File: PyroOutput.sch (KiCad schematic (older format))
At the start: 9 parts, among them J11 PYRO 1, U11 TPS1HC100

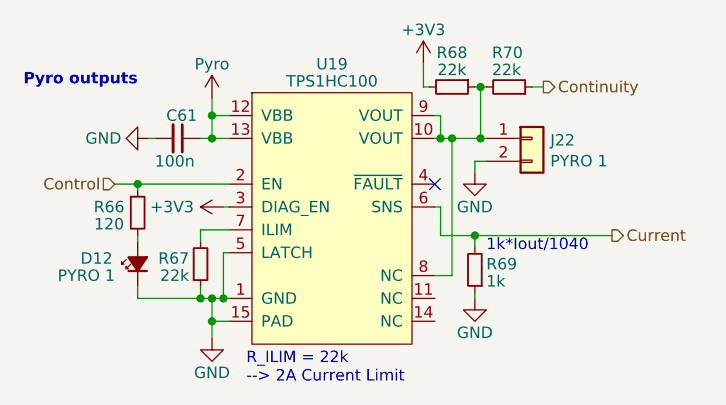
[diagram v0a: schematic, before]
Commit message: changed form factor to better fit into uHb engine section
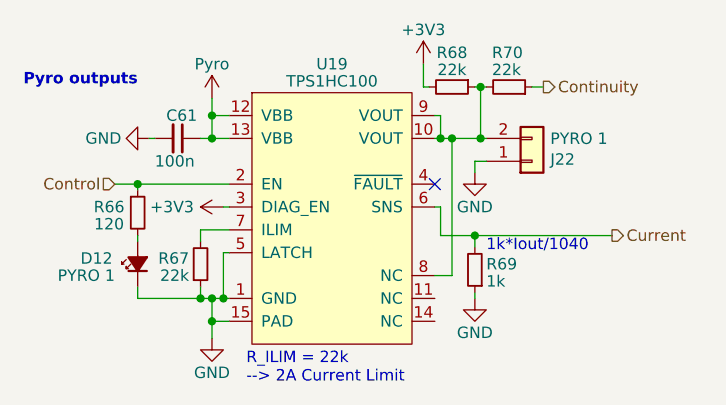
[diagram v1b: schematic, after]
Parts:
- J11: footprint TXV_LIB:Molex_SL_1x2 -> TXV_LIB:Molex_SL_1x2_Vertical
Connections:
- net GND: now also J11.1 (Pin_1); no longer J11.2 (Pin_2)
- net at R34.1, R36.2, U11.10 (VOUT)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: now also J11.2 (Pin_2); no longer J11.1 (Pin_1)
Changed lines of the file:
@@
 L Connector_Generic:Conn_01x02 J?
 U 1 1 639C46E3
-P 6550 3875
+P 6550 3975
 AR Path="/639C46E3" Ref="J?"  Part="1"
 AR Path="/638A960E/639C46E3" Ref="J11"  Part="1"
 AR Path="/64156100/639C46E3" Ref="J21"  Part="1"
 AR Path="/6419F64A/639C46E3" Ref="J22"  Part="1"
-F 0 "J22" H 6630 3867 50  0000 L CNN
-F 1 "PYRO 1" H 6630 3776 50  0000 L CNN
-F 2 "TXV_LIB:Molex_SL_1x2" H 6550 3875 50  0001 C CNN
-F 3 "" H 6550 3875 50  0001 C CNN
-F 4 "" H 6550 3875 50  0001 C CNN "Male Mate"
-F 5 "" H 6550 3875 50  0001 C CNN "Mate Datasheet"
-	1    6550 3875
-	1    0    0    -1
+F 0 "J22" H 6630 3967 50  0000 L CNN
+F 1 "PYRO 1" H 6630 3876 50  0000 L CNN
+F 2 "TXV_LIB:Molex_SL_1x2_Vertical" H 6550 3975 50  0001 C CNN
+F 3 "" H 6550 3975 50  0001 C CNN
+F 4 "" H 6550 3975 50  0001 C CNN "Male Mate"
+F 5 "" H 6550 3975 50  0001 C CNN "Mate Datasheet"
+	1    6550 3975
+	1    0    0    1
 $EndComp
 Text HLabel 4725 4075 0    50   Input ~ 0

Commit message: moved 7V4 buck to separate board
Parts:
- R36: value 22k -> 100k
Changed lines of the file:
@@
 $Descr A4 11693 8268
 encoding utf-8
-Sheet 17 17
+Sheet 6 17
 Title ""
 Date ""
@@
 AR Path="/64156100/639C464D" Ref="R64"  Part="1"
 AR Path="/6419F64A/639C464D" Ref="R69"  Part="1"
-F 0 "R69" H 6250 4425 50  0000 R CNN
+F 0 "R35" H 6250 4425 50  0000 R CNN
 F 1 "1k" H 6250 4500 50  0000 R CNN
 F 2 "Resistor_SMD:R_0603_1608Metric" H 6300 4450 50  0001 C CNN
@@
 AR Path="/64156100/639C4656" Ref="#PWR0180"  Part="1"
 AR Path="/6419F64A/639C4656" Ref="#PWR0187"  Part="1"
-F 0 "#PWR0187" H 4875 3625 50  0001 C CNN
+F 0 "#PWR0123" H 4875 3625 50  0001 C CNN
 F 1 "GND" V 4875 3675 50  0000 C CNN
 F 2 "" H 4875 3875 50  0001 C CNN
@@
 AR Path="/64156100/639C465D" Ref="#PWR0181"  Part="1"
 AR Path="/6419F64A/639C465D" Ref="#PWR0188"  Part="1"
-F 0 "#PWR0188" H 5150 3550 50  0001 C CNN
+F 0 "#PWR0124" H 5150 3550 50  0001 C CNN
 F 1 "Pyro" H 5150 3850 50  0000 C CNN
 F 2 "" H 5150 3700 50  0001 C CNN
@@
 AR Path="/64156100/639C4663" Ref="C60"  Part="1"
 AR Path="/6419F64A/639C4663" Ref="C61"  Part="1"
-F 0 "C61" V 4900 3825 50  0000 L CNN
+F 0 "C45" V 4900 3825 50  0000 L CNN
 F 1 "100n" V 5100 3775 50  0000 L CNN
 F 2 "Capacitor_SMD:C_0402_1005Metric" H 5000 3875 50  0001 C CNN
@@
 AR Path="/64156100/639C466C" Ref="#PWR0182"  Part="1"
 AR Path="/6419F64A/639C466C" Ref="#PWR0189"  Part="1"
-F 0 "#PWR0189" H 5200 4025 50  0001 C CNN
+F 0 "#PWR0125" H 5200 4025 50  0001 C CNN
 F 1 "+3V3" V 5200 4400 50  0000 C CNN
 F 2 "" H 5200 4175 50  0001 C CNN
@@
 AR Path="/64156100/639C4675" Ref="R62"  Part="1"
 AR Path="/6419F64A/639C4675" Ref="R67"  Part="1"
-F 0 "R67" H 5050 4400 50  0000 R CNN
+F 0 "R33" H 5050 4400 50  0000 R CNN
 F 1 "22k" H 5050 4475 50  0000 R CNN
 F 2 "Resistor_SMD:R_0603_1608Metric" H 5100 4425 50  0001 C CNN
@@
 AR Path="/64156100/639C468D" Ref="#PWR0183"  Part="1"
 AR Path="/6419F64A/639C468D" Ref="#PWR0190"  Part="1"
-F 0 "#PWR0190" H 6300 4325 50  0001 C CNN
+F 0 "#PWR0126" H 6300 4325 50  0001 C CNN
 F 1 "GND" H 6300 4425 50  0000 C CNN
 F 2 "" H 6300 4575 50  0001 C CNN
@@
 AR Path="/64156100/639C469C" Ref="U18"  Part="1"
 AR Path="/6419F64A/639C469C" Ref="U19"  Part="1"
-F 0 "U19" H 5675 4900 50  0000 C CNN
+F 0 "U11" H 5675 4900 50  0000 C CNN
 F 1 "TPS1HC100" H 5675 4825 50  0000 C CNN
 F 2 "Package_SO:HTSSOP-14-1EP_4.4x5mm_P0.65mm_EP3.4x5mm_Mask3x3.1mm" H 5675 3575 50  0001 C CNN
@@
 AR Path="/64156100/639C46A2" Ref="R61"  Part="1"
 AR Path="/6419F64A/639C46A2" Ref="R66"  Part="1"
-F 0 "R66" H 4700 4225 50  0000 C CNN
+F 0 "R32" H 4700 4225 50  0000 C CNN
 F 1 "120" H 4700 4150 50  0000 C CNN
 F 2 "Resistor_SMD:R_0603_1608Metric" H 4825 4200 50  0001 C CNN
@@
 AR Path="/64156100/639C46AD" Ref="R65"  Part="1"
 AR Path="/6419F64A/639C46AD" Ref="R70"  Part="1"
-F 0 "R70" V 6600 3575 50  0000 L CNN
-F 1 "22k" V 6525 3575 50  0000 L CNN
+F 0 "R36" V 6600 3575 50  0000 L CNN
+F 1 "100k" V 6525 3575 50  0000 L CNN
 F 2 "Resistor_SMD:R_0603_1608Metric" H 6450 3650 50  0001 C CNN
 F 3 "~" H 6450 3650 50  0001 C CNN
@@
 AR Path="/64156100/639C46B3" Ref="R63"  Part="1"
 AR Path="/6419F64A/639C46B3" Ref="R68"  Part="1"
-F 0 "R68" V 6050 3650 50  0000 C CNN
+F 0 "R34" V 6050 3650 50  0000 C CNN
 F 1 "22k" V 6125 3650 50  0000 C CNN
 F 2 "Resistor_SMD:R_0603_1608Metric" H 6200 3650 50  0001 C CNN
@@
 AR Path="/64156100/639C46B9" Ref="#PWR0184"  Part="1"
 AR Path="/6419F64A/639C46B9" Ref="#PWR0191"  Part="1"
-F 0 "#PWR0191" H 6075 3400 50  0001 C CNN
+F 0 "#PWR0127" H 6075 3400 50  0001 C CNN
 F 1 "+3V3" H 6075 3700 50  0000 C CNN
 F 2 "" H 6075 3550 50  0001 C CNN
@@
 AR Path="/64156100/639C46CD" Ref="#PWR0185"  Part="1"
 AR Path="/6419F64A/639C46CD" Ref="#PWR0192"  Part="1"
-F 0 "#PWR0192" H 6300 3775 50  0001 C CNN
+F 0 "#PWR0128" H 6300 3775 50  0001 C CNN
 F 1 "GND" H 6300 3875 50  0000 C CNN
 F 2 "" H 6300 4025 50  0001 C CNN
@@
 AR Path="/64156100/639C46D4" Ref="#PWR0186"  Part="1"
 AR Path="/6419F64A/639C46D4" Ref="#PWR0193"  Part="1"
-F 0 "#PWR0193" H 5150 4500 50  0001 C CNN
+F 0 "#PWR0129" H 5150 4500 50  0001 C CNN
 F 1 "GND" H 5150 4600 50  0000 C CNN
 F 2 "" H 5150 4750 50  0001 C CNN
@@
 AR Path="/64156100/639C46DA" Ref="D11"  Part="1"
 AR Path="/6419F64A/639C46DA" Ref="D12"  Part="1"
-F 0 "D12" V 4850 4675 50  0000 R CNN
+F 0 "D8" V 4850 4675 50  0000 R CNN
 F 1 "PYRO 1" V 4775 4775 50  0000 R CNN
 F 2 "LED_SMD:LED_0603_1608Metric" V 4825 4425 50  0001 C CNN
@@
 AR Path="/64156100/639C46E3" Ref="J21"  Part="1"
 AR Path="/6419F64A/639C46E3" Ref="J22"  Part="1"
-F 0 "J22" H 6630 3967 50  0000 L CNN
+F 0 "J11" H 6630 3967 50  0000 L CNN
 F 1 "PYRO 1" H 6630 3876 50  0000 L CNN
 F 2 "TXV_LIB:Molex_SL_1x2_Vertical" H 6550 3975 50  0001 C CNN

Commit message: many small changes, before removing servo buck converter
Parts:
- R33: value 22k -> 56k
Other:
- note added: "R_ILIM = 56k\n--> 860mA Current Limit"
- note removed: "R_ILIM = 22k\n--> 2A Current Limit"
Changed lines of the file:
@@
 $EndComp
 Text Notes 5300 4950 0    50   ~ 0
-R_ILIM = 22k\n--> 2A Current Limit
+R_ILIM = 56k\n--> 860mA Current Limit
 Text Notes 6350 4375 0    50   ~ 0
 1k*Iout/1040
@@
 AR Path="/6419F64A/639C4675" Ref="R67"  Part="1"
 F 0 "R33" H 5050 4400 50  0000 R CNN
-F 1 "22k" H 5050 4475 50  0000 R CNN
+F 1 "56k" H 5050 4475 50  0000 R CNN
 F 2 "Resistor_SMD:R_0603_1608Metric" H 5100 4425 50  0001 C CNN
 F 3 "~" H 5100 4425 50  0001 C CNN

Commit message: placement almost done
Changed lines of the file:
@@
 $Descr A4 11693 8268
 encoding utf-8
-Sheet 6 17
+Sheet 17 18
 Title ""
 Date ""
@@
 AR Path="/64156100/639C464D" Ref="R64"  Part="1"
 AR Path="/6419F64A/639C464D" Ref="R69"  Part="1"
-F 0 "R35" H 6250 4425 50  0000 R CNN
+F 0 "R69" H 6250 4425 50  0000 R CNN
 F 1 "1k" H 6250 4500 50  0000 R CNN
 F 2 "Resistor_SMD:R_0603_1608Metric" H 6300 4450 50  0001 C CNN
@@
 AR Path="/64156100/639C4656" Ref="#PWR0180"  Part="1"
 AR Path="/6419F64A/639C4656" Ref="#PWR0187"  Part="1"
-F 0 "#PWR0123" H 4875 3625 50  0001 C CNN
+F 0 "#PWR0187" H 4875 3625 50  0001 C CNN
 F 1 "GND" V 4875 3675 50  0000 C CNN
 F 2 "" H 4875 3875 50  0001 C CNN
@@
 AR Path="/64156100/639C465D" Ref="#PWR0181"  Part="1"
 AR Path="/6419F64A/639C465D" Ref="#PWR0188"  Part="1"
-F 0 "#PWR0124" H 5150 3550 50  0001 C CNN
+F 0 "#PWR0188" H 5150 3550 50  0001 C CNN
 F 1 "Pyro" H 5150 3850 50  0000 C CNN
 F 2 "" H 5150 3700 50  0001 C CNN
@@
 AR Path="/64156100/639C4663" Ref="C60"  Part="1"
 AR Path="/6419F64A/639C4663" Ref="C61"  Part="1"
-F 0 "C45" V 4900 3825 50  0000 L CNN
+F 0 "C61" V 4900 3825 50  0000 L CNN
 F 1 "100n" V 5100 3775 50  0000 L CNN
 F 2 "Capacitor_SMD:C_0402_1005Metric" H 5000 3875 50  0001 C CNN
@@
 AR Path="/64156100/639C466C" Ref="#PWR0182"  Part="1"
 AR Path="/6419F64A/639C466C" Ref="#PWR0189"  Part="1"
-F 0 "#PWR0125" H 5200 4025 50  0001 C CNN
+F 0 "#PWR0189" H 5200 4025 50  0001 C CNN
 F 1 "+3V3" V 5200 4400 50  0000 C CNN
 F 2 "" H 5200 4175 50  0001 C CNN
@@
 AR Path="/64156100/639C4675" Ref="R62"  Part="1"
 AR Path="/6419F64A/639C4675" Ref="R67"  Part="1"
-F 0 "R33" H 5050 4400 50  0000 R CNN
+F 0 "R67" H 5050 4400 50  0000 R CNN
 F 1 "56k" H 5050 4475 50  0000 R CNN
 F 2 "Resistor_SMD:R_0603_1608Metric" H 5100 4425 50  0001 C CNN
@@
 AR Path="/64156100/639C468D" Ref="#PWR0183"  Part="1"
 AR Path="/6419F64A/639C468D" Ref="#PWR0190"  Part="1"
-F 0 "#PWR0126" H 6300 4325 50  0001 C CNN
+F 0 "#PWR0190" H 6300 4325 50  0001 C CNN
 F 1 "GND" H 6300 4425 50  0000 C CNN
 F 2 "" H 6300 4575 50  0001 C CNN
@@
 AR Path="/64156100/639C469C" Ref="U18"  Part="1"
 AR Path="/6419F64A/639C469C" Ref="U19"  Part="1"
-F 0 "U11" H 5675 4900 50  0000 C CNN
+F 0 "U19" H 5675 4900 50  0000 C CNN
 F 1 "TPS1HC100" H 5675 4825 50  0000 C CNN
 F 2 "Package_SO:HTSSOP-14-1EP_4.4x5mm_P0.65mm_EP3.4x5mm_Mask3x3.1mm" H 5675 3575 50  0001 C CNN
@@
 AR Path="/64156100/639C46A2" Ref="R61"  Part="1"
 AR Path="/6419F64A/639C46A2" Ref="R66"  Part="1"
-F 0 "R32" H 4700 4225 50  0000 C CNN
+F 0 "R66" H 4700 4225 50  0000 C CNN
 F 1 "120" H 4700 4150 50  0000 C CNN
 F 2 "Resistor_SMD:R_0603_1608Metric" H 4825 4200 50  0001 C CNN
@@
 AR Path="/64156100/639C46AD" Ref="R65"  Part="1"
 AR Path="/6419F64A/639C46AD" Ref="R70"  Part="1"
-F 0 "R36" V 6600 3575 50  0000 L CNN
+F 0 "R70" V 6600 3575 50  0000 L CNN
 F 1 "100k" V 6525 3575 50  0000 L CNN
 F 2 "Resistor_SMD:R_0603_1608Metric" H 6450 3650 50  0001 C CNN
@@
 AR Path="/64156100/639C46B3" Ref="R63"  Part="1"
 AR Path="/6419F64A/639C46B3" Ref="R68"  Part="1"
-F 0 "R34" V 6050 3650 50  0000 C CNN
+F 0 "R68" V 6050 3650 50  0000 C CNN
 F 1 "22k" V 6125 3650 50  0000 C CNN
 F 2 "Resistor_SMD:R_0603_1608Metric" H 6200 3650 50  0001 C CNN
@@
 AR Path="/64156100/639C46B9" Ref="#PWR0184"  Part="1"
 AR Path="/6419F64A/639C46B9" Ref="#PWR0191"  Part="1"
-F 0 "#PWR0127" H 6075 3400 50  0001 C CNN
+F 0 "#PWR0191" H 6075 3400 50  0001 C CNN
 F 1 "+3V3" H 6075 3700 50  0000 C CNN
 F 2 "" H 6075 3550 50  0001 C CNN
@@
 AR Path="/64156100/639C46CD" Ref="#PWR0185"  Part="1"
 AR Path="/6419F64A/639C46CD" Ref="#PWR0192"  Part="1"
-F 0 "#PWR0128" H 6300 3775 50  0001 C CNN
+F 0 "#PWR0192" H 6300 3775 50  0001 C CNN
 F 1 "GND" H 6300 3875 50  0000 C CNN
 F 2 "" H 6300 4025 50  0001 C CNN
@@
 AR Path="/64156100/639C46D4" Ref="#PWR0186"  Part="1"
 AR Path="/6419F64A/639C46D4" Ref="#PWR0193"  Part="1"
-F 0 "#PWR0129" H 5150 4500 50  0001 C CNN
+F 0 "#PWR0193" H 5150 4500 50  0001 C CNN
 F 1 "GND" H 5150 4600 50  0000 C CNN
 F 2 "" H 5150 4750 50  0001 C CNN
@@
 AR Path="/64156100/639C46DA" Ref="D11"  Part="1"
 AR Path="/6419F64A/639C46DA" Ref="D12"  Part="1"
-F 0 "D8" V 4850 4675 50  0000 R CNN
+F 0 "D12" V 4850 4675 50  0000 R CNN
 F 1 "PYRO 1" V 4775 4775 50  0000 R CNN
 F 2 "LED_SMD:LED_0603_1608Metric" V 4825 4425 50  0001 C CNN
@@
 AR Path="/64156100/639C46E3" Ref="J21"  Part="1"
 AR Path="/6419F64A/639C46E3" Ref="J22"  Part="1"
-F 0 "J11" H 6630 3967 50  0000 L CNN
+F 0 "J22" H 6630 3967 50  0000 L CNN
 F 1 "PYRO 1" H 6630 3876 50  0000 L CNN
 F 2 "TXV_LIB:Molex_SL_1x2_Vertical" H 6550 3975 50  0001 C CNN

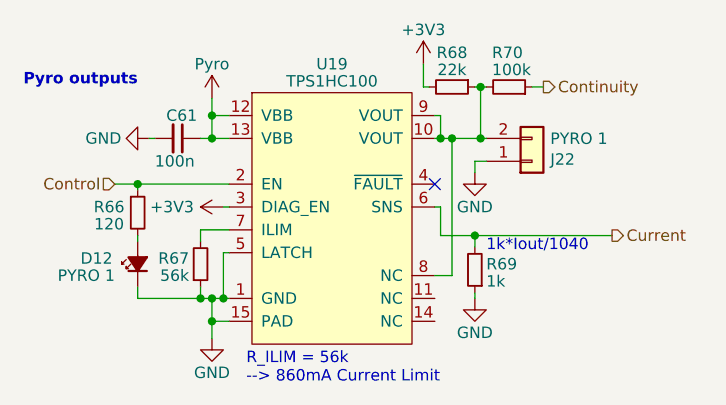
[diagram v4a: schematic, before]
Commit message: fixed net names
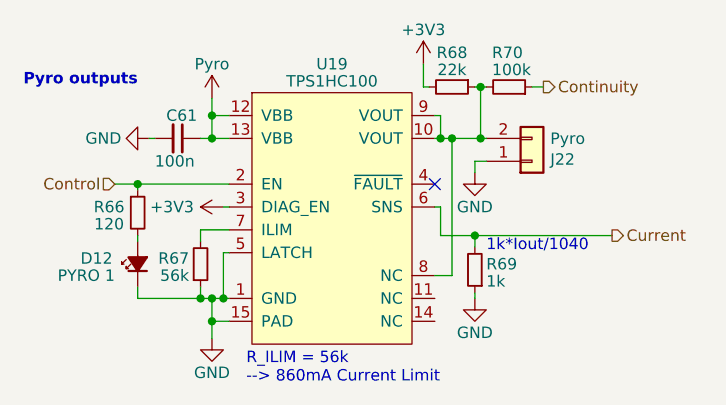
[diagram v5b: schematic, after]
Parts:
- J11: value PYRO 1 -> Pyro
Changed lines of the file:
@@
 AR Path="/6419F64A/639C46E3" Ref="J22"  Part="1"
 F 0 "J22" H 6630 3967 50  0000 L CNN
-F 1 "PYRO 1" H 6630 3876 50  0000 L CNN
+F 1 "Pyro" H 6630 3876 50  0000 L CNN
 F 2 "TXV_LIB:Molex_SL_1x2_Vertical" H 6550 3975 50  0001 C CNN
 F 3 "" H 6550 3975 50  0001 C CNN

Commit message: schematic done, preliminary placement done
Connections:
- no-connect marks 1 -> 3
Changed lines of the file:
@@
 $Descr A4 11693 8268
 encoding utf-8
-Sheet 17 18
+Sheet 6 18
 Title ""
 Date ""
@@
 AR Path="/64156100/639C464D" Ref="R64"  Part="1"
 AR Path="/6419F64A/639C464D" Ref="R69"  Part="1"
-F 0 "R69" H 6250 4425 50  0000 R CNN
+F 0 "R35" H 6250 4425 50  0000 R CNN
 F 1 "1k" H 6250 4500 50  0000 R CNN
 F 2 "Resistor_SMD:R_0603_1608Metric" H 6300 4450 50  0001 C CNN
@@
 AR Path="/64156100/639C4663" Ref="C60"  Part="1"
 AR Path="/6419F64A/639C4663" Ref="C61"  Part="1"
-F 0 "C61" V 4900 3825 50  0000 L CNN
+F 0 "C45" V 4900 3825 50  0000 L CNN
 F 1 "100n" V 5100 3775 50  0000 L CNN
 F 2 "Capacitor_SMD:C_0402_1005Metric" H 5000 3875 50  0001 C CNN
@@
 AR Path="/64156100/639C4675" Ref="R62"  Part="1"
 AR Path="/6419F64A/639C4675" Ref="R67"  Part="1"
-F 0 "R67" H 5050 4400 50  0000 R CNN
+F 0 "R33" H 5050 4400 50  0000 R CNN
 F 1 "56k" H 5050 4475 50  0000 R CNN
 F 2 "Resistor_SMD:R_0603_1608Metric" H 5100 4425 50  0001 C CNN
@@
 AR Path="/64156100/639C469C" Ref="U18"  Part="1"
 AR Path="/6419F64A/639C469C" Ref="U19"  Part="1"
-F 0 "U19" H 5675 4900 50  0000 C CNN
+F 0 "U11" H 5675 4900 50  0000 C CNN
 F 1 "TPS1HC100" H 5675 4825 50  0000 C CNN
 F 2 "Package_SO:HTSSOP-14-1EP_4.4x5mm_P0.65mm_EP3.4x5mm_Mask3x3.1mm" H 5675 3575 50  0001 C CNN
@@
 AR Path="/64156100/639C46A2" Ref="R61"  Part="1"
 AR Path="/6419F64A/639C46A2" Ref="R66"  Part="1"
-F 0 "R66" H 4700 4225 50  0000 C CNN
+F 0 "R32" H 4700 4225 50  0000 C CNN
 F 1 "120" H 4700 4150 50  0000 C CNN
 F 2 "Resistor_SMD:R_0603_1608Metric" H 4825 4200 50  0001 C CNN
@@
 AR Path="/64156100/639C46AD" Ref="R65"  Part="1"
 AR Path="/6419F64A/639C46AD" Ref="R70"  Part="1"
-F 0 "R70" V 6600 3575 50  0000 L CNN
+F 0 "R36" V 6600 3575 50  0000 L CNN
 F 1 "100k" V 6525 3575 50  0000 L CNN
 F 2 "Resistor_SMD:R_0603_1608Metric" H 6450 3650 50  0001 C CNN
@@
 AR Path="/64156100/639C46B3" Ref="R63"  Part="1"
 AR Path="/6419F64A/639C46B3" Ref="R68"  Part="1"
-F 0 "R68" V 6050 3650 50  0000 C CNN
+F 0 "R34" V 6050 3650 50  0000 C CNN
 F 1 "22k" V 6125 3650 50  0000 C CNN
 F 2 "Resistor_SMD:R_0603_1608Metric" H 6200 3650 50  0001 C CNN
@@
 AR Path="/64156100/639C46DA" Ref="D11"  Part="1"
 AR Path="/6419F64A/639C46DA" Ref="D12"  Part="1"
-F 0 "D12" V 4850 4675 50  0000 R CNN
+F 0 "D8" V 4850 4675 50  0000 R CNN
 F 1 "PYRO 1" V 4775 4775 50  0000 R CNN
 F 2 "LED_SMD:LED_0603_1608Metric" V 4825 4425 50  0001 C CNN
@@
 AR Path="/64156100/639C46E3" Ref="J21"  Part="1"
 AR Path="/6419F64A/639C46E3" Ref="J22"  Part="1"
-F 0 "J22" H 6630 3967 50  0000 L CNN
+F 0 "J11" H 6630 3967 50  0000 L CNN
 F 1 "Pyro" H 6630 3876 50  0000 L CNN
 F 2 "TXV_LIB:Molex_SL_1x2_Vertical" H 6550 3975 50  0001 C CNN
@@
 Text HLabel 6900 4300 2    50   Output ~ 0
 Current
+NoConn ~ 6125 4575
+NoConn ~ 6125 4675
 $EndSCHEMATC

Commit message: routing started
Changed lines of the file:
@@
 $Descr A4 11693 8268
 encoding utf-8
-Sheet 6 18
+Sheet 14 18
 Title ""
 Date ""
@@
 AR Path="/64156100/639C464D" Ref="R64"  Part="1"
 AR Path="/6419F64A/639C464D" Ref="R69"  Part="1"
-F 0 "R35" H 6250 4425 50  0000 R CNN
+F 0 "R64" H 6250 4425 50  0000 R CNN
 F 1 "1k" H 6250 4500 50  0000 R CNN
 F 2 "Resistor_SMD:R_0603_1608Metric" H 6300 4450 50  0001 C CNN
@@
 AR Path="/64156100/639C4656" Ref="#PWR0180"  Part="1"
 AR Path="/6419F64A/639C4656" Ref="#PWR0187"  Part="1"
-F 0 "#PWR0187" H 4875 3625 50  0001 C CNN
+F 0 "#PWR0180" H 4875 3625 50  0001 C CNN
 F 1 "GND" V 4875 3675 50  0000 C CNN
 F 2 "" H 4875 3875 50  0001 C CNN
@@
 AR Path="/64156100/639C465D" Ref="#PWR0181"  Part="1"
 AR Path="/6419F64A/639C465D" Ref="#PWR0188"  Part="1"
-F 0 "#PWR0188" H 5150 3550 50  0001 C CNN
+F 0 "#PWR0181" H 5150 3550 50  0001 C CNN
 F 1 "Pyro" H 5150 3850 50  0000 C CNN
 F 2 "" H 5150 3700 50  0001 C CNN
@@
 AR Path="/64156100/639C4663" Ref="C60"  Part="1"
 AR Path="/6419F64A/639C4663" Ref="C61"  Part="1"
-F 0 "C45" V 4900 3825 50  0000 L CNN
+F 0 "C60" V 4900 3825 50  0000 L CNN
 F 1 "100n" V 5100 3775 50  0000 L CNN
 F 2 "Capacitor_SMD:C_0402_1005Metric" H 5000 3875 50  0001 C CNN
@@
 AR Path="/64156100/639C466C" Ref="#PWR0182"  Part="1"
 AR Path="/6419F64A/639C466C" Ref="#PWR0189"  Part="1"
-F 0 "#PWR0189" H 5200 4025 50  0001 C CNN
+F 0 "#PWR0182" H 5200 4025 50  0001 C CNN
 F 1 "+3V3" V 5200 4400 50  0000 C CNN
 F 2 "" H 5200 4175 50  0001 C CNN
@@
 AR Path="/64156100/639C4675" Ref="R62"  Part="1"
 AR Path="/6419F64A/639C4675" Ref="R67"  Part="1"
-F 0 "R33" H 5050 4400 50  0000 R CNN
+F 0 "R62" H 5050 4400 50  0000 R CNN
 F 1 "56k" H 5050 4475 50  0000 R CNN
 F 2 "Resistor_SMD:R_0603_1608Metric" H 5100 4425 50  0001 C CNN
@@
 AR Path="/64156100/639C468D" Ref="#PWR0183"  Part="1"
 AR Path="/6419F64A/639C468D" Ref="#PWR0190"  Part="1"
-F 0 "#PWR0190" H 6300 4325 50  0001 C CNN
+F 0 "#PWR0183" H 6300 4325 50  0001 C CNN
 F 1 "GND" H 6300 4425 50  0000 C CNN
 F 2 "" H 6300 4575 50  0001 C CNN
@@
 AR Path="/64156100/639C469C" Ref="U18"  Part="1"
 AR Path="/6419F64A/639C469C" Ref="U19"  Part="1"
-F 0 "U11" H 5675 4900 50  0000 C CNN
+F 0 "U18" H 5675 4900 50  0000 C CNN
 F 1 "TPS1HC100" H 5675 4825 50  0000 C CNN
 F 2 "Package_SO:HTSSOP-14-1EP_4.4x5mm_P0.65mm_EP3.4x5mm_Mask3x3.1mm" H 5675 3575 50  0001 C CNN
@@
 AR Path="/64156100/639C46A2" Ref="R61"  Part="1"
 AR Path="/6419F64A/639C46A2" Ref="R66"  Part="1"
-F 0 "R32" H 4700 4225 50  0000 C CNN
+F 0 "R61" H 4700 4225 50  0000 C CNN
 F 1 "120" H 4700 4150 50  0000 C CNN
 F 2 "Resistor_SMD:R_0603_1608Metric" H 4825 4200 50  0001 C CNN
@@
 AR Path="/64156100/639C46AD" Ref="R65"  Part="1"
 AR Path="/6419F64A/639C46AD" Ref="R70"  Part="1"
-F 0 "R36" V 6600 3575 50  0000 L CNN
+F 0 "R65" V 6600 3575 50  0000 L CNN
 F 1 "100k" V 6525 3575 50  0000 L CNN
 F 2 "Resistor_SMD:R_0603_1608Metric" H 6450 3650 50  0001 C CNN
@@
 AR Path="/64156100/639C46B3" Ref="R63"  Part="1"
 AR Path="/6419F64A/639C46B3" Ref="R68"  Part="1"
-F 0 "R34" V 6050 3650 50  0000 C CNN
+F 0 "R63" V 6050 3650 50  0000 C CNN
 F 1 "22k" V 6125 3650 50  0000 C CNN
 F 2 "Resistor_SMD:R_0603_1608Metric" H 6200 3650 50  0001 C CNN
@@
 AR Path="/64156100/639C46B9" Ref="#PWR0184"  Part="1"
 AR Path="/6419F64A/639C46B9" Ref="#PWR0191"  Part="1"
-F 0 "#PWR0191" H 6075 3400 50  0001 C CNN
+F 0 "#PWR0184" H 6075 3400 50  0001 C CNN
 F 1 "+3V3" H 6075 3700 50  0000 C CNN
 F 2 "" H 6075 3550 50  0001 C CNN
@@
 AR Path="/64156100/639C46CD" Ref="#PWR0185"  Part="1"
 AR Path="/6419F64A/639C46CD" Ref="#PWR0192"  Part="1"
-F 0 "#PWR0192" H 6300 3775 50  0001 C CNN
+F 0 "#PWR0185" H 6300 3775 50  0001 C CNN
 F 1 "GND" H 6300 3875 50  0000 C CNN
 F 2 "" H 6300 4025 50  0001 C CNN
@@
 AR Path="/64156100/639C46D4" Ref="#PWR0186"  Part="1"
 AR Path="/6419F64A/639C46D4" Ref="#PWR0193"  Part="1"
-F 0 "#PWR0193" H 5150 4500 50  0001 C CNN
+F 0 "#PWR0186" H 5150 4500 50  0001 C CNN
 F 1 "GND" H 5150 4600 50  0000 C CNN
 F 2 "" H 5150 4750 50  0001 C CNN
@@
 AR Path="/64156100/639C46DA" Ref="D11"  Part="1"
 AR Path="/6419F64A/639C46DA" Ref="D12"  Part="1"
-F 0 "D8" V 4850 4675 50  0000 R CNN
+F 0 "D11" V 4850 4675 50  0000 R CNN
 F 1 "PYRO 1" V 4775 4775 50  0000 R CNN
 F 2 "LED_SMD:LED_0603_1608Metric" V 4825 4425 50  0001 C CNN
@@
 AR Path="/64156100/639C46E3" Ref="J21"  Part="1"
 AR Path="/6419F64A/639C46E3" Ref="J22"  Part="1"
-F 0 "J11" H 6630 3967 50  0000 L CNN
+F 0 "J21" H 6630 3967 50  0000 L CNN
 F 1 "Pyro" H 6630 3876 50  0000 L CNN
 F 2 "TXV_LIB:Molex_SL_1x2_Vertical" H 6550 3975 50  0001 C CNN
